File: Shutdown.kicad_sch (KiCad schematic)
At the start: 87 parts, among them J1 DRC23-24PA, J2 0430450629, Q13 SI2347DS-T1-GE3, Q15 SI2347DS-T1-GE3, Q16 SI2347DS-T1-GE3, Q18 SI2318CDS-T1-GE3, Q19 SI2318CDS-T1-GE3, Q20 SI2347DS-T1-GE3, Q23 SI2318CDS-T1-GE3, Q4 SI2347DS-T1-GE3, Q5 SI2318CDS-T1-GE3, Q6 SI2347DS-T1-GE3, Q8 SI2347DS-T1-GE3

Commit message: completed schematic cleanup, back on 12V
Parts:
- removed C10, C9: 100nF, Capacitor_SMD:C_0603_1608Metric_Pad1.08x0.95mm_HandSolder, symbol -C-Ceramic-0603:C-0603-100nF-10%-50V-X7R
- removed D1, D25, D28, D30, D31, D32, D33, D34, D7, D8: Red, LED_SMD:LED_0805_2012Metric, symbol -Diodes-LED:NCD0805R1
- removed D2, D23, D24, D26: BZT52C16, Diode_SMD:D_SOD-123, symbol -Diodes-Zener:BZT52C16
- removed J1: DRC23-24PA, -Connectors:DRC2324PB, symbol -Connectors:DRC23-24PA
- removed J2: 0430450629, -Connectors:CONN_SD-43045-010_06_MOL, symbol -Connectors:0430450629
- removed Q13, Q15, Q16, Q8: SI2347DS-T1-GE3, Package_TO_SOT_SMD:SOT-23-3, symbol -MOSFET-P-Channel:SI2347DS-T1-GE3
- removed R14, R17, R19, R20, R21, R3, R39, R4, R5: 100k, Resistor_SMD:R_0603_1608Metric_Pad0.98x0.95mm_HandSolder, symbol -R-SMD-0603:R-0603-100k-1%-100mW-100PPM
- removed R23, R40, R41, R42, R47, R63, R64, R65, R66, R67: 510, Resistor_SMD:R_0603_1608Metric_Pad0.98x0.95mm_HandSolder, symbol -R-SMD-0603:R-0603-510-1%-100mW-100PPM
- removed TP5, TP6, TP7, TP8: ~, TestPoint:TestPoint_Pad_1.0x1.0mm, symbol -Test-Points:Square-Pad-1mm
- added C1, C2: 10uF, Capacitor_SMD:C_0603_1608Metric_Pad1.08x0.95mm_HandSolder, symbol -C-Ceramic-0603:C-0603-10uF-20%-25V-X5R
- added J3: 348302001, -Connectors:348302001, symbol -Connectors:348302001
- added J4: 348300801, -Connectors:348300801, symbol -Connectors:348300801
- renumbered C1 to C3, D17 to D1, D19 to D10, D22 to D11, D29 to D2, D44 to D3, D27 to D4, D6 to D5, D45 to D6, D18 to D7, D21 to D8, D20 to D9, Q20 to Q1, Q23 to Q2, Q18 to Q3, Q6 to Q4, Q4 to Q6, Q19 to Q7, R12 to R1, R33 to R10, R32 to R11, R1 to R12, R37 to R13, R35 to R14, R34 to R15, R7 to R17, R38 to R18, R85 to R2, R84 to R3, R18 to R4, R93 to R5, R57 to R6, R48 to R7, R94 to R8, R95 to R9, TP25 to TP1, TP1 to TP2, TP2 to TP3, TP3 to TP4, TP4 to TP5
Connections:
- net BMS-OUT is gone; now on net BMS-FAULT: R8.2, R9.2
- net IMD-OUT is gone; now on net IMD-FAULT: R10.2, R11.2
- net BATT+: now also J4.5, J4.6
- net BMS-FAULT: now also J3.8
- net BOTS-A: now also J3.14
- net BOTS-B: now also J3.15
- net GND: now also C1.1, C2.1, J4.4, J4.7, J4.8
- net HVILS-A: now also J3.3; no longer Q6.3 (D), R18.2, TP5.1
- net IMD-FAULT: now also J3.9
- net BMS-Fault-Passthru/ERROR-SIG renamed BMS-FAULT-VCU
- net BYPASS renamed BYPASS-BTN
- net BYPASS-BTN: now also J3.2
- net IMD-Fault-Passthru/ERROR-SIG renamed IMD-FAULT-VCU
- new net BMS-FAULT-VCU-BUF: J3.12
- new net BSE: C2.2, J3.18
- new net BSPD-FAULT-VCU-BUF: J3.11
- new net CRASH-SW-A: J3.16
- new net CRASH-SW-B: J3.17
- new net HVILS-B: J3.4
- new net IMD-FAULT-VCU-BUF: J3.13
- new net ISENSE-EXT: C1.2, J3.7
- new net SD-POWER: J4.1, J4.2, J4.3
- new net Shutdown-Circuit/POWER-IN: Q6.3 (D), R18.2, TP5.1
- new net TSMS-A: J3.5
- new net TSMS-B: J3.6
- new net TSSI-STATUS: J3.1
- no-connect marks 0 -> 3
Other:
- added sheet Buffered-Faults (Buffered-Faults.kicad_sch)
- added sheet Shutdown-Circuit (Shutdown-Circuit.kicad_sch)
- sheet BMS-Fault-Passthru ports: added none; removed ERROR-OUT
- sheet BSPD-Fault-Passthru ports: added none; removed ERROR-OUT
- sheet BSPD-Logic ports: added BSE, ISENSE-EXT; removed ACCUM-VOUT, BRAKE-VOUT
- sheet IMD-Fault-Passthru ports: added none; removed ERROR-OUT
- sheet Indicator-Lights ports: added BMS-FAULT-VCU, IMD-FAULT-VCU, TSSI-STATUS; removed BMS-FAULT, IMD-FAULT, STATUS
- note added: "Buffered Fault Signals"
- note added: "Indicator Lights"
- note added: "Input Power"
- note removed: "BSPD Logic"
- note removed: "Indicator LEDs"
- note removed: "Reverse Polarity and Overvoltage Protection"
- note removed: "Shutdown Circuit"
- moved on the sheet: C3, D1, D10, D11, D2, D3, D4, D5, D6, D7, D8, D9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

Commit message: completed placement:
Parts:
- added MH1, MH2, MH3, MH4: ~, MountingHole:MountingHole_3.5mm_Pad_TopBottom, symbol -Mounting-Hole:M3 3.5mm Ø
- renumbered D2 to D1, D11 to D10, D8 to D11, D3 to D2, D4 to D3, D5 to D4, D1 to D5, D10 to D6, D6 to D7, D7 to D8, J3 to J1, J4 to J2, Q6 to Q2, Q2 to Q3, Q3 to Q4, Q7 to Q6, Q4 to Q7, R3 to R1, R16 to R10, R8 to R11, R10 to R12, R9 to R13, R11 to R14, R13 to R15, R14 to R16, R12 to R17, R17 to R18, R4 to R2, R5 to R3, R6 to R4, R7 to R5, R2 to R6, R1 to R7, R18 to R8, R15 to R9
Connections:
- net BATT+: now also J2.1, J2.2; no longer J2.5, J2.6
- net GND: now also J2.3; no longer J2.7
- net SD-POWER: now also J2.5, J2.6, J2.7; no longer J2.1, J2.2, J2.3
- no-connect marks 3 -> 7
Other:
- note added: "Mounting"

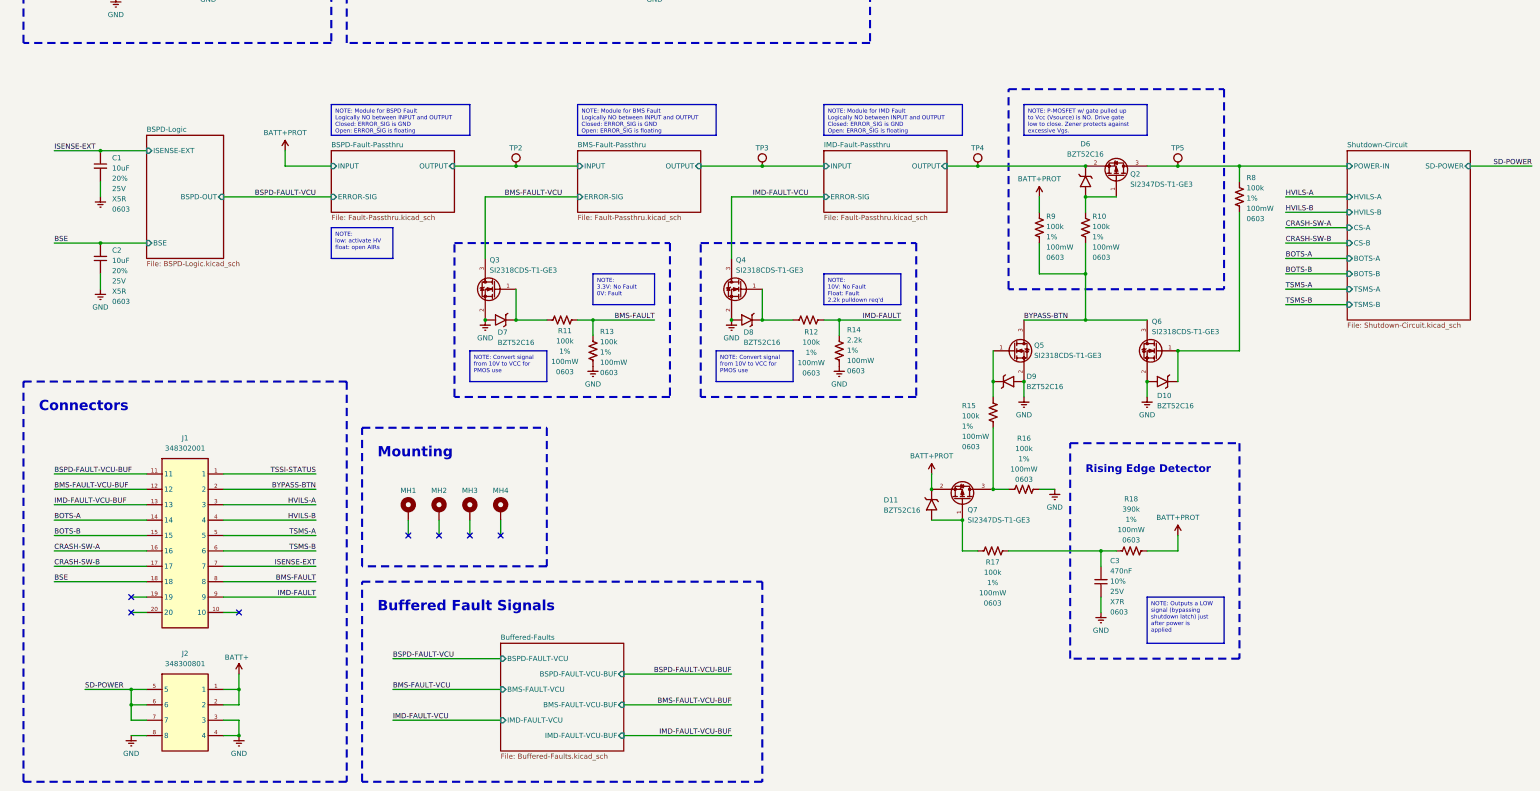
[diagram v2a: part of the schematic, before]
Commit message: changed BSPD, BMS fault logic to match Mk11 specs, all signals going back to VCU have 12V fault, 0V no fault readings, connector symbols/footprints left for next push
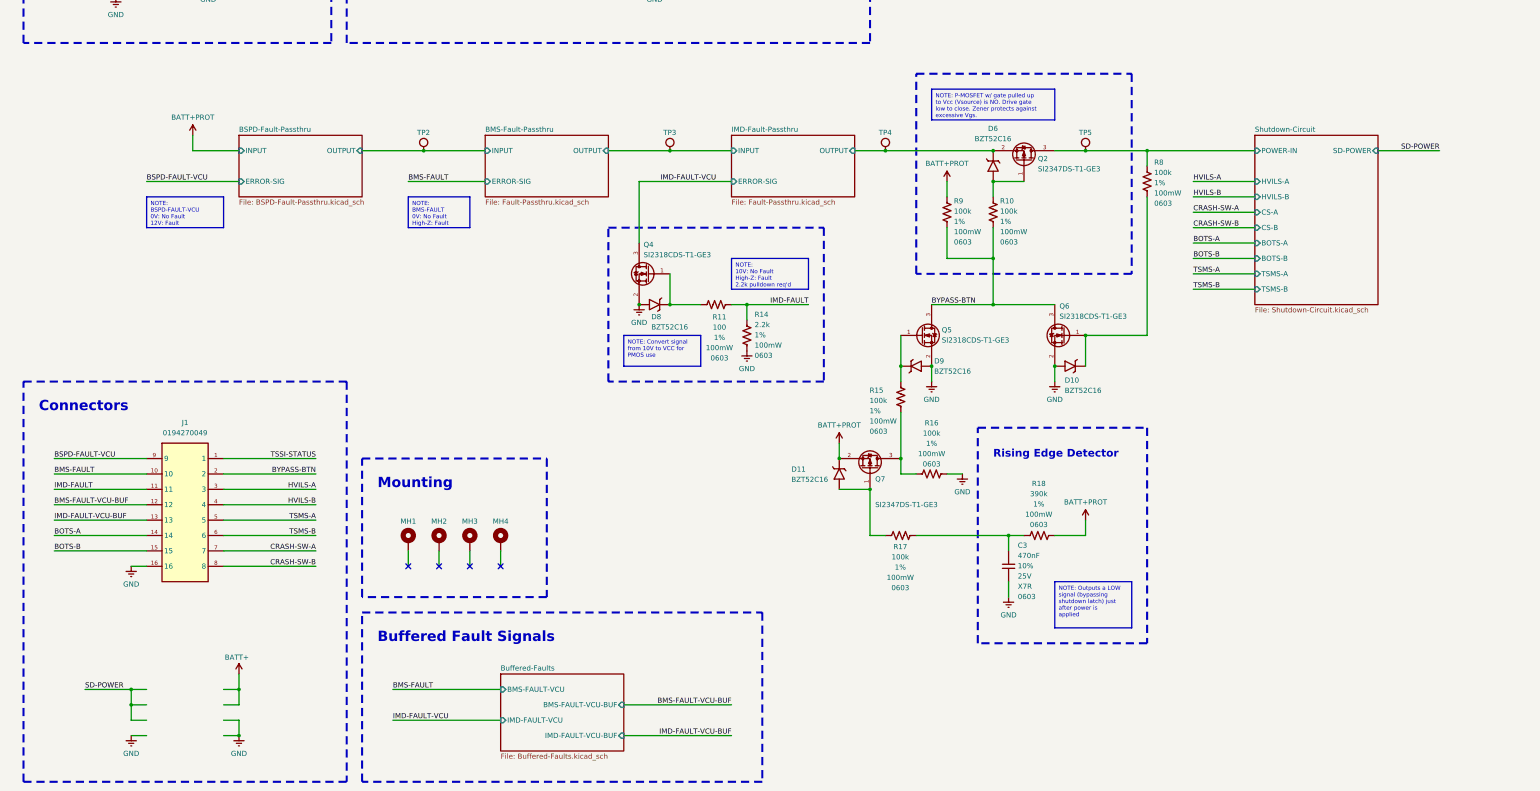
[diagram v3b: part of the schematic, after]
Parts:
- removed C1, C2: 10uF, Capacitor_SMD:C_0603_1608Metric_Pad1.08x0.95mm_HandSolder, symbol -C-Ceramic-0603:C-0603-10uF-20%-25V-X5R
- removed D7: BZT52C16, Diode_SMD:D_SOD-123, symbol -Diodes-Zener:BZT52C16
- removed J1: 348302001, -Connectors:348302001, symbol -Connectors:348302001
- removed J2: 348300801, -Connectors:348300801, symbol -Connectors:348300801
- removed Q3: SI2318CDS-T1-GE3, Package_TO_SOT_SMD:SOT-23-3, symbol -MOSFET-N-Channel:SI2318CDS-T1-GE3
- removed R11, R12, R13: 100k, Resistor_SMD:R_0603_1608Metric_Pad0.98x0.95mm_HandSolder, symbol -R-SMD-0603:R-0603-100k-1%-100mW-100PPM
- added J1: 0194270049, -Connectors:0194270049, symbol -Connectors:0194270049
- added R11: 100, Resistor_SMD:R_0603_1608Metric_Pad0.98x0.95mm_HandSolder, symbol -R-SMD-0603:R-0603-100-1%-100mW-100PPM
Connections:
- net BMS-FAULT: now also J1.10
- net BMS-FAULT-VCU-BUF: now also J1.12
- net BOTS-A: now also J1.14
- net BOTS-B: now also J1.15
- net BSPD-FAULT-VCU: now also J1.9
- net BYPASS-BTN: now also J1.2
- net CRASH-SW-A: now also J1.7
- net CRASH-SW-B: now also J1.8
- net GND: now also J1.16
- net HVILS-A: now also J1.3
- net HVILS-B: now also J1.4
- net IMD-FAULT: now also J1.11, R11.2
- net IMD-FAULT-VCU-BUF: now also J1.13
- net TSMS-A: now also J1.5
- net TSMS-B: now also J1.6
- net TSSI-STATUS: now also J1.1
- net at D8.1 (K), Q4.1 (G): now also R11.1
- no-connect marks 7 -> 4
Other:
- removed sheet BSPD-Logic
- sheet BSPD-Fault-Passthru: file Fault-Passthru.kicad_sch -> BSPD-Fault-Passthru.kicad_sch
- sheet Buffered-Faults ports: added none; removed BSPD-FAULT-VCU, BSPD-FAULT-VCU-BUF
- moved on the sheet: C3, D10, D11, D6, D8, D9, MH1, MH2, MH3, MH4, Q2, Q4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
